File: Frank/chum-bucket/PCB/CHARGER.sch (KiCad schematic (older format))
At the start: 34 parts

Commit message: minor schematic update + inrush sim
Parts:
- added C? (x2): 0.1uF, symbol Device:C_Small
- added R? (x4): 0, symbol Device:R
- added U? (x2): INA196, Package_TO_SOT_SMD:SOT-23-5, symbol Amplifier_Current:INA196
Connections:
- net labels added: +3.3V, ANALOG_I_CHG, ANALOG_I_SYS, I_CHG_JMP_N, I_CHG_JMP_P, I_SYS_JMP_N, I_SYS_JMP_P
- wire segments 104 -> 124
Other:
- note added: "- Current amplifiers are 20V/V\n- Expected max output voltage is 2V (10A)\n- Protection and filtering on MCU page\n- Jumpers placed in case input impedance\n in case input impedance is too low \n and trips the charger"
- moved on the sheet: C?, D?, L?, Q?, R?, U?

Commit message: Weekends work. Final component selection then ready for review :)
huge oof
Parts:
- removed C?: 0.1uF, symbol Device:C_Small
- removed C?: 0.1u, symbol Device:C_Small
- removed D? (x2): BU, symbol Device:LED_Small
- removed Q?: Q_NMOS_DGS, symbol Device:Q_NMOS_DGS
- removed Q?: Q_PMOS_DGS, symbol Device:Q_PMOS_DGS
- removed R? (x2): 0, symbol Device:R
- removed R?: 1k, symbol Device:R_Small
- removed R?: 100k, symbol Device:R_Small
- removed U?: INA196, Package_TO_SOT_SMD:SOT-23-5, symbol Amplifier_Current:INA196
- added C? (x3): 100nF, symbol Device:C_Small
- added C?: 22nF, symbol Device:C_Small
- added C?: C, symbol Device:C_Small
- added D? (x2): GN, LED_SMD:LED_0603_1608Metric, symbol Device:LED_Small
- added F?: Fuse, symbol Device:Fuse
- added Q?: 2N7002K, Package_TO_SOT_SMD:SOT-23, symbol Transistor_FET:2N7002K
- added Q?: BSS84, Package_TO_SOT_SMD:SOT-23, symbol Transistor_FET:BSS84
- added R?: 330, symbol Device:R
- added R?: 100, symbol Device:R
- added R?: 4.7k, symbol Device:R_Small
- added R?: 1k, symbol Device:R_Small
- added R?: 10k, symbol Device:R_Small
- added R?: 430k, symbol Device:R
- added R?: 9.31k, symbol Device:R
- added R?: 5.1k, symbol Device:R
- added R?: 1k, symbol Device:R
- added R? (x2): 0, symbol Device:R_Small
- added TH?: NTC_TERM, Resistor_SMD:R_0603_1608Metric, symbol Device:Thermistor_NTC
- added U?: BTS6142DAUMA1, Package_TO_SOT_SMD:TO-252-4, symbol chum-bucket:BTS6142DAUMA1
- C?: value C_Small -> 1uF
- D?: value BU -> GN; footprint (none) -> LED_SMD:LED_0603_1608Metric; Digikey (none) -> 732-4971-2-ND
- R? (x2): value 100k -> 4.7k; Tolerance (none) -> 0.1%
- R?: value 32.4k -> 4.7k; Tolerance (none) -> 0.1%
- R?: value 100k -> ??; Tolerance (none) -> 0.1%
- R?: value 32.4k -> ??; Tolerance (none) -> 0.1%
- R?: value 32.4k -> 6.8k; Tolerance (none) -> 0.1%
- R?: value R -> 10m
- R? (x3): value 10k -> 1k
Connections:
- net labels added: +3V3, +BATT, AC_DRV, VREF, ~AC_DRV, ~BQ24617_BATT_DRV, ~CHG_LS_EN
- net labels removed: I_SYS_JMP_N, I_SYS_JMP_P
- wire segments 124 -> 164
- no-connect marks 0 -> 2
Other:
- note added: "- Current amplifier is 20V/V\n- Expected max output voltage is 2V (10A)\n- Protection and filtering on MCU page\n- Jumpers place in case BQ current sense input impedance is low"
- note added: "Final charge voltage set using this voltage divider\nV_bat = 2.1 * (1+R_top/R_bot)\nV_bat = 4.2*3 = 12.6\n12.6 * 2.1 - 1 = 5 = R_top/R_bot"
- note added: "Inverter glue logic for charger IC to supply load switch"
- note added: "Max IS current is 10mA under fault.\n330 ohm means max voltage of 3.1V"
- note added: "Option for thermistor. \nDNC for initial build\nVoltage div is dummy therm for testing"
- note added: "RIN_1 controls slew\nrate of the system bus"
- note added: "TTC pin sets time limit on charge\n0.01uF = 1 hour\n0.11uF = 10 hours\n5.6 min/nF\nCells should be 0.5C charge so we gucci w/ 2 hour"
- note removed: "- Current amplifiers are 20V/V\n- Expected max output voltage is 2V (10A)\n- Protection and filtering on MCU page\n- Jumpers placed in case input impedance\n in case input impedance is too low \n and trips the charger"
- note removed: "To do: Convert to load switch, use glue logic w/ stm"
- note removed: "To do: add load switch to turn pack onto system rail"
- moved on the sheet: C?, R?, U?

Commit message: batt-management sheet updates
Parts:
- added C? (x3): 10u, symbol Device:C_Small
- gave numbers to parts that had none: 1
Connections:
- wire segments 164 -> 173
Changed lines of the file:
@@
 SYS_PWR_OUT
 Wire Wire Line
-	4300 1100 6700 1100
+	4300 1100 5550 1100
 Wire Wire Line
 	4000 2050 4000 1100
@@
 ANALOG_I_SYS
 $Comp
-L Device:R R?
+L Device:R RIN_1
 U 1 1 5F19E549
 P 1600 6500
-F 0 "R?" H 1670 6546 50  0000 L CNN
+F 0 "RIN_1" H 1670 6546 50  0000 L CNN
 F 1 "100" H 1670 6455 50  0000 L CNN
 F 2 "" V 1530 6500 50  0001 C CNN
@@
 	-1   0    0    1
 $EndComp
+Wire Wire Line
+	6150 1450 6150 1400
+Wire Wire Line
+	5850 1450 5850 1400
+Wire Wire Line
+	5550 1450 5550 1400
+$Comp
+L power:GND #PWR?
+U 1 1 5F305781
+P 6150 1450
+AR Path="/5ECF1AA9/5F305781" Ref="#PWR?"  Part="1"
+AR Path="/5F305781" Ref="#PWR?"  Part="1"
+F 0 "#PWR?" H 6150 1200 50  0001 C CNN
+F 1 "GND" H 6155 1277 50  0000 C CNN
+F 2 "" H 6150 1450 50  0001 C CNN
+F 3 "" H 6150 1450 50  0001 C CNN
+	1    6150 1450
+	1    0    0    -1
+$EndComp
+$Comp
+L power:GND #PWR?
+U 1 1 5F305787
+P 5850 1450
+AR Path="/5ECF1AA9/5F305787" Ref="#PWR?"  Part="1"
+AR Path="/5F305787" Ref="#PWR?"  Part="1"
+F 0 "#PWR?" H 5850 1200 50  0001 C CNN
+F 1 "GND" H 5855 1277 50  0000 C CNN
+F 2 "" H 5850 1450 50  0001 C CNN
+F 3 "" H 5850 1450 50  0001 C CNN
+	1    5850 1450
+	1    0    0    -1
+$EndComp
+$Comp
+L power:GND #PWR?
+U 1 1 5F30578D
+P 5550 1450
+AR Path="/5ECF1AA9/5F30578D" Ref="#PWR?"  Part="1"
+AR Path="/5F30578D" Ref="#PWR?"  Part="1"
+F 0 "#PWR?" H 5550 1200 50  0001 C CNN
+F 1 "GND" H 5555 1277 50  0000 C CNN
+F 2 "" H 5550 1450 50  0001 C CNN
+F 3 "" H 5550 1450 50  0001 C CNN
+	1    5550 1450
+	1    0    0    -1
+$EndComp
+$Comp
+L Device:C_Small C?
+U 1 1 5F305793
+P 6150 1300
+AR Path="/5ECF1AA9/5F305793" Ref="C?"  Part="1"
+AR Path="/5F305793" Ref="C?"  Part="1"
+F 0 "C?" H 6058 1254 50  0000 R CNN
+F 1 "10u" H 6058 1345 50  0000 R CNN
+F 2 "" H 6150 1300 50  0001 C CNN
+F 3 "~" H 6150 1300 50  0001 C CNN
+	1    6150 1300
+	1    0    0    1
+$EndComp
+$Comp
+L Device:C_Small C?
+U 1 1 5F305799
+P 5850 1300
+AR Path="/5ECF1AA9/5F305799" Ref="C?"  Part="1"
+AR Path="/5F305799" Ref="C?"  Part="1"
+F 0 "C?" H 5758 1254 50  0000 R CNN
+F 1 "10u" H 5758 1345 50  0000 R CNN
+F 2 "" H 5850 1300 50  0001 C CNN
+F 3 "~" H 5850 1300 50  0001 C CNN
+	1    5850 1300
+	1    0    0    1
+$EndComp
+$Comp
+L Device:C_Small C?
+U 1 1 5F30579F
+P 5550 1300
+AR Path="/5ECF1AA9/5F30579F" Ref="C?"  Part="1"
+AR Path="/5F30579F" Ref="C?"  Part="1"
+F 0 "C?" H 5458 1254 50  0000 R CNN
+F 1 "10u" H 5458 1345 50  0000 R CNN
+F 2 "" H 5550 1300 50  0001 C CNN
+F 3 "~" H 5550 1300 50  0001 C CNN
+	1    5550 1300
+	1    0    0    1
+$EndComp
+Wire Wire Line
+	5550 1200 5550 1100
+Connection ~ 5550 1100
+Wire Wire Line
+	5550 1100 5850 1100
+Wire Wire Line
+	5850 1200 5850 1100
+Connection ~ 5850 1100
+Wire Wire Line
+	5850 1100 6150 1100
+Wire Wire Line
+	6150 1200 6150 1100
+Connection ~ 6150 1100
+Wire Wire Line
+	6150 1100 6700 1100
 $EndSCHEMATC

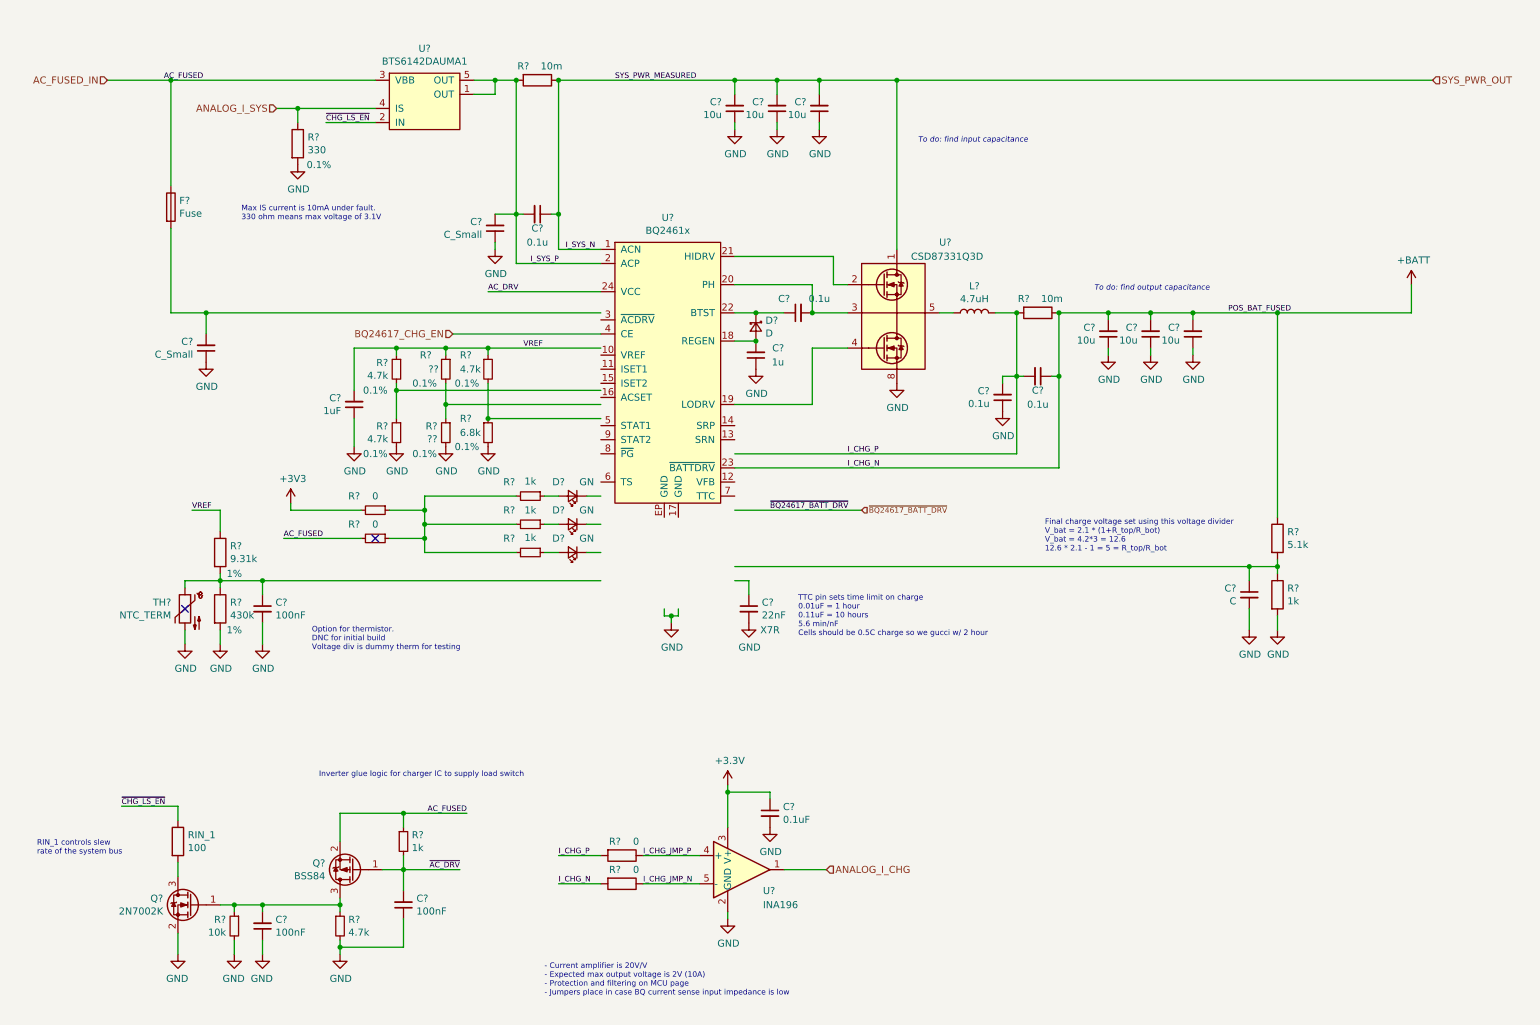
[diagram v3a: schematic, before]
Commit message: Minor schematic organization changes
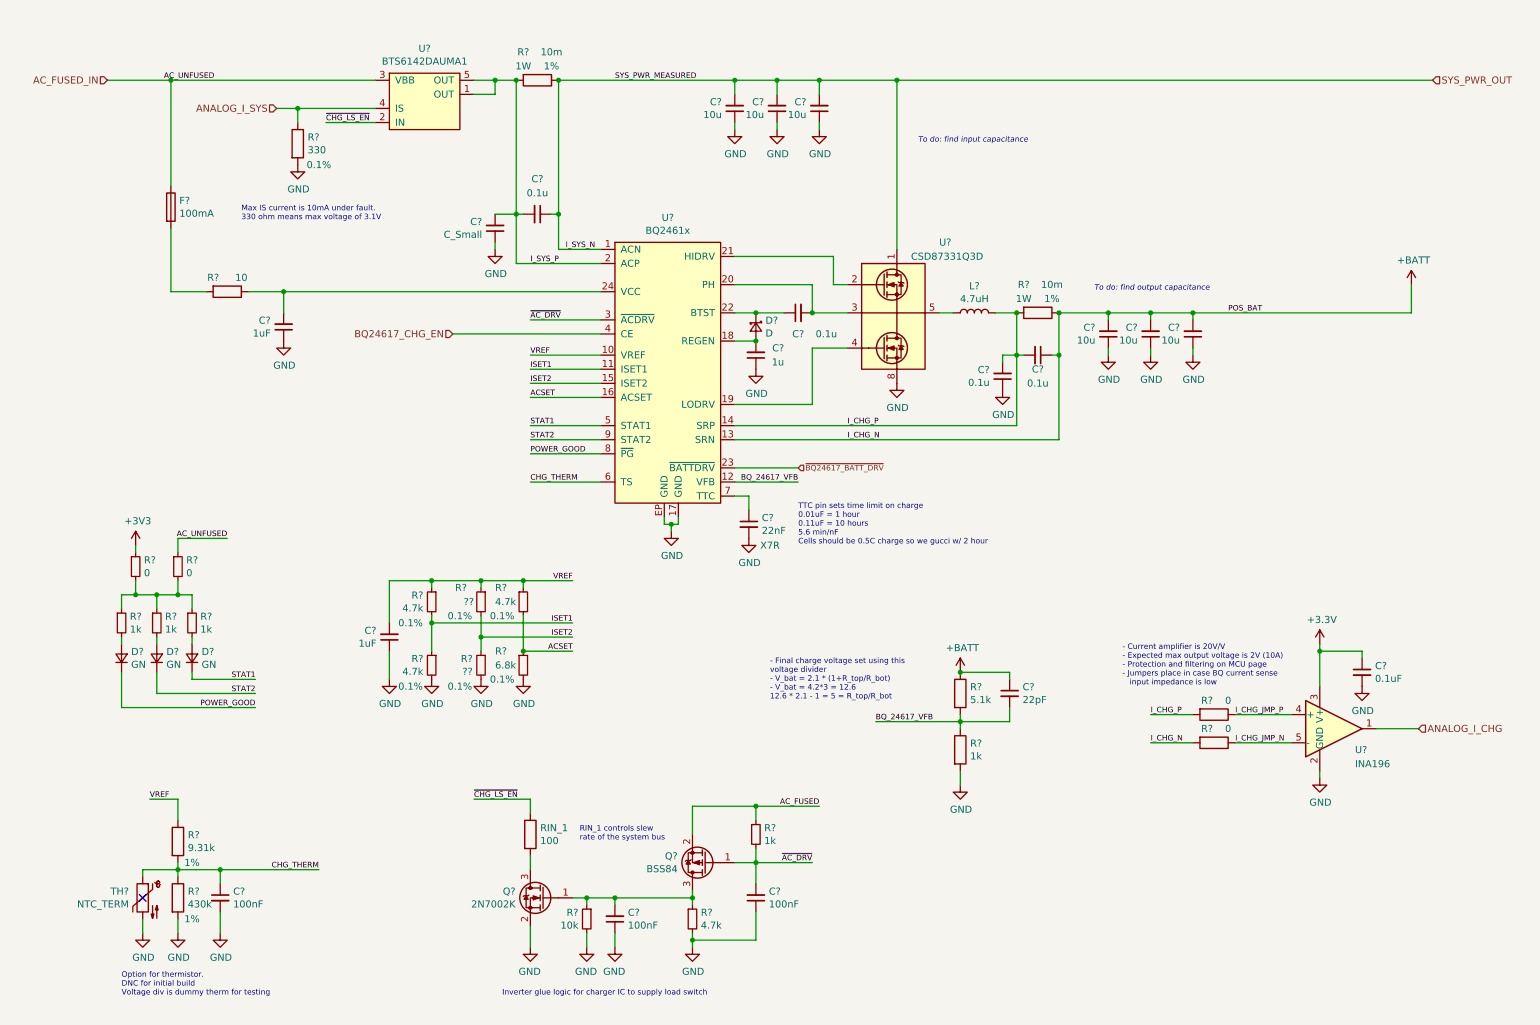
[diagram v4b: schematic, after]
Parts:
- removed D? (x3): GN, LED_SMD:LED_0603_1608Metric, symbol Device:LED_Small
- removed R? (x2): 0, symbol Device:R_Small
- removed R?: 10m, symbol Device:R
- removed R? (x3): 1k, symbol Device:R_Small
- added D? (x3): GN, symbol Device:D_Small
- added R? (x2): 0, symbol Device:R_Small
- added R? (x3): 1k, symbol Device:R_Small
- added R?: 10, symbol Device:R
- added R?: 10m, Resistor_SMD:R_2512_6332Metric_Pad1.52x3.35mm_HandSolder, symbol Device:R
- C?: value C -> 22pF
- C?: value C_Small -> 1uF
- F?: value Fuse -> 100mA
- R?: footprint (none) -> Resistor_SMD:R_2512_6332Metric_Pad1.52x3.35mm_HandSolder; Digikey (none) -> YAG2167TR-ND; Power (none) -> 1W; Tolerancw (none) -> 1%
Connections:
- net labels added: ACSET, AC_UNFUSED, BQ_24617_VFB, CHG_THERM, ISET1, ISET2, POS_BAT, POWER_GOOD, STAT1, STAT2
- net labels removed: AC_DRV, POS_BAT_FUSED
- wire segments 173 -> 185
- no-connect marks 2 -> 1
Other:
- note added: "- Current amplifier is 20V/V\n- Expected max output voltage is 2V (10A)\n- Protection and filtering on MCU page\n- Jumpers place in case BQ current sense \n input impedance is low"
- note added: "- Final charge voltage set using this \nvoltage divider\n- V_bat = 2.1 * (1+R_top/R_bot)\n- V_bat = 4.2*3 = 12.6\n12.6 * 2.1 - 1 = 5 = R_top/R_bot"
- note removed: "- Current amplifier is 20V/V\n- Expected max output voltage is 2V (10A)\n- Protection and filtering on MCU page\n- Jumpers place in case BQ current sense input impedance is low"
- note removed: "Final charge voltage set using this voltage divider\nV_bat = 2.1 * (1+R_top/R_bot)\nV_bat = 4.2*3 = 12.6\n12.6 * 2.1 - 1 = 5 = R_top/R_bot"
- moved on the sheet: C?, Q?, R?, RIN_1, TH?, U?

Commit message: for review at 2pm
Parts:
- removed C? (x6): 10u, symbol Device:C_Small
- removed R?: 10m, Resistor_SMD:R_2512_6332Metric_Pad1.52x3.35mm_HandSolder, symbol Device:R
- added C? (x9): 4.7uF, Capacitor_SMD:C_1210_3225Metric, symbol Device:C_Small
- added R?: 10m, Resistor_SMD:R_1206_3216Metric, symbol Device:R
- C?: value 1u -> 1uF; Voltage (none) -> 6V
- R?: footprint Resistor_SMD:R_2512_6332Metric_Pad1.52x3.35mm_HandSolder -> Resistor_SMD:R_1206_3216Metric; Digikey YAG2167TR-ND -> CRF1206-FZ-R010ELFTR-ND
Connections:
- net +BATT: now also C?.2, C?.2, C?.2, R?.1
- net GND: now also C?.1, C?.1, C?.1, C?.1, C?.1, C?.1, C?.1, C?.1, C?.1
- net I_CHG_P: now also R?.2
- net SYS_PWR_OUT: now also C?.2, C?.2, C?.2, C?.2, C?.2, C?.2
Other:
- note removed: "To do: find input capacitance"
- note removed: "To do: find output capacitance"

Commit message: more work
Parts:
- removed C? (x9): 4.7uF, Capacitor_SMD:C_1210_3225Metric, symbol Device:C_Small
- removed C?: 0.1uF, symbol Device:C_Small
- removed C? (x2): 100nF, symbol Device:C_Small
- removed C?: 1uF, symbol Device:C_Small
- removed C? (x2): 0.1u, symbol Device:C_Small
- removed D? (x2): GN, symbol Device:D_Small
- removed R?: 0, symbol Device:R_Small
- removed R? (x3): 1k, symbol Device:R_Small
- removed R?: 10k, symbol Device:R_Small
- removed R?: ??, symbol Device:R_Small
- removed R?: 4.7k, symbol Device:R_Small
- added C101: 1uF, Capacitor_SMD:C_0805_2012Metric, symbol Device:C_Small
- added C106, C110, C112, C116, C117: 10uF, Capacitor_SMD:C_2220_5650Metric, symbol Device:C
- added C108, C113, C114: 0.1uF, Capacitor_SMD:C_0603_1608Metric, symbol Device:C_Small
- added C115: 0.1u, Capacitor_SMD:C_0603_1608Metric, symbol Device:C_Small
- added C118: 10nF, Capacitor_SMD:C_0603_1608Metric, symbol Device:C_Small
- added D102, D103: GN, LED_SMD:LED_0603_1608Metric, symbol Device:D_Small
- added R105, R108: 10k, Resistor_SMD:R_0603_1608Metric, symbol Device:R_Small
- added R113, R115, R123, R125: 1k, Resistor_SMD:R_0603_1608Metric, symbol Device:R_Small
- added R114: 0, Resistor_SMD:R_0603_1608Metric, symbol Device:R_Small
- added R121: 100, Resistor_SMD:R_0603_1608Metric, symbol Device:R
- C102: renamed from C?; footprint (none) -> Capacitor_SMD:C_0603_1608Metric; Digikey (none) -> 399-7874-2-ND; Voltage (none) -> 25V
- C103: renamed from C?; footprint (none) -> Capacitor_SMD:C_0805_2012Metric; Voltage (none) -> 25V
- C104: renamed from C?; value C_Small -> 0.1uF; footprint (none) -> Capacitor_SMD:C_0603_1608Metric; Digikey (none) -> 399-7845-2-ND
- C105: renamed from C?; footprint (none) -> Capacitor_SMD:C_0603_1608Metric; Digikey (none) -> 399-7845-2-ND
- C107: renamed from C?; footprint (none) -> Capacitor_SMD:C_0805_2012Metric; Digikey (none) -> 490-1644-2-ND; Tolerance X7R -> C0G
- C109: renamed from C?; footprint (none) -> Capacitor_SMD:C_0805_2012Metric
- C111: renamed from C?; footprint (none) -> Capacitor_SMD:C_0603_1608Metric; Digikey (none) -> 399-7845-2-ND; Voltage (none) -> 25V
- C119: renamed from C?; value 100nF -> 10nF; footprint (none) -> Capacitor_SMD:C_0603_1608Metric; Digikey (none) -> 399-7842-2-ND; Voltage (none) -> 25V
- D101: renamed from D?; footprint (none) -> LED_SMD:LED_0603_1608Metric; Digikey (none) -> 160-1446-2-ND
- D104: renamed from D?; value D -> BAT54T1G; footprint (none) -> Diode_SMD:D_SOD-123F; Digikey (none) -> BAT54T1GOSTR-ND
- F101: renamed from F?; footprint (none) -> Fuse:Fuse_0603_1608Metric; Digikey (none) -> 478-6872-2-ND
- R101: renamed from R?; value 4.7k -> 10k; footprint (none) -> Resistor_SMD:R_0603_1608Metric
- R102: renamed from R?; value 4.7k -> 3.3k
- R103: renamed from R?; value 5.1k -> 499k; footprint (none) -> Resistor_SMD:R_0603_1608Metric; Tolerance (none) -> 0.1%
- R104: renamed from R?; value 1k -> 100k; footprint (none) -> Resistor_SMD:R_0603_1608Metric; Tolerance (none) -> 0.1%
- R106: renamed from R?; value ?? -> 330
- R107: renamed from R?; footprint (none) -> Resistor_SMD:R_0603_1608Metric; Digikey (none) -> 541-10UATR-ND; Power (none) -> 0.1W
- R109: renamed from R?; value 6.8k -> 15k
- R110: renamed from R?; footprint (none) -> Resistor_SMD:R_0603_1608Metric; Digikey (none) -> P19915TR-ND; Power (none) -> 0.1W
- R111, R112, R117, R118, R119, R120: renamed from R?; footprint (none) -> Resistor_SMD:R_0603_1608Metric
- R124: renamed from R?; footprint (none) -> Resistor_SMD:R_0603_1608Metric; Digikey (none) -> RHM4.7DTR-ND
- RIN_1: footprint (none) -> Resistor_SMD:R_0603_1608Metric; Digikey (none) -> 311-100HRTR-ND; Percentage 0.1% -> 1%
- gave numbers to parts that had none: 10
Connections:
- net +3V3: now also C108.2
- net +BATT: now also C115.1, C116.1, C117.1
- net ACSET: now also R108.2
- net AC_FUSED: now also R125.1
- net AC_FUSED_IN: now also R114.1
- net CHG_THERM: now also C113.2, R121.2; no longer R119.2, R120.1, TH101.1
- net GND: now also C101.1, C106.2, C108.1, C110.2, C112.2, C113.1, C114.1, C116.2, C117.2, C118.1, R123.2
- net ISET2: now also R105.2
- net I_CHG_P: now also C114.2, C115.2
- net STAT1: now also D103.1 (K)
- net STAT2: now also D102.1 (K)
- net SYS_PWR_OUT: now also C106.1, C110.1, C112.1
- net VREF: now also C101.2, R105.1, R108.1
- net ~AC_DRV: now also R125.2
- net at Q101.1 (G), Q102.3 (D), R124.1: now also C118.2, R123.1
- net at R111.1, R112.2: now also R113.1, R114.2, R115.1
- new net: D102.2 (A), R113.2
- new net: D103.2 (A), R115.2
- new net: R119.2, R120.1, R121.1, TH101.1
- no-connect marks 1 -> 2
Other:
- note added: "- Current amplifier is 20V/V\n- Expected max output voltage is 2V (10A)\n- Protection and filtering on MCU page\n- Jumpers place in case BQ current sense \n input impedance is low\n- Bandwidth of 500kHz so may alias waveform"
- note added: "- ISET1 sets max current during charge (0.5C*8A = 4A)\n- ISET2 sets precharge AND termination charge current (100mA)\n- ACSET sets the max AC adapter current (10A)"
- note added: "- VREF = 3.3V\n- V_ISET1 = I_CHG * 20 * RSR = 0.8V\n- V_ISET2 = I_TERM * 100 * RSR = 0.1V\n- V_ACSET = I_AC * 20 * R_AC = 2V"
- note added: "<----- Load Switch | Charger IC ----->"
- note added: "Option for thermistor. \nDNC for initial build\nJust pop. voltage div. as dummy therm. \nFilter 3db freq: 16kHz"
- note added: "Option to choose LED power. \nUse 10kOhm for AC_Adapter"
- note added: "VCC max current is 25mA\nI^R = .025*.025*10 < 0.1W"
- note removed: "- Current amplifier is 20V/V\n- Expected max output voltage is 2V (10A)\n- Protection and filtering on MCU page\n- Jumpers place in case BQ current sense \n input impedance is low"
- note removed: "Option for thermistor. \nDNC for initial build\nVoltage div is dummy therm for testing"
- moved on the sheet: C102, C119, D101, Q101, Q102, R101, R102, R103, R104, R106, R109, R111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

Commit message: changes
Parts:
- added TP? (x2): VFB, TestPoint:TestPoint_Pad_D1.0mm, symbol Connector:TestPoint
- added TP?: SW_NODE, TestPoint:TestPoint_Pad_D1.0mm, symbol Connector:TestPoint
- U103: value CSD87331Q3D -> CSD87331
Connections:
- net BQ_24617_VFB: now also TP?.1
- net CHG_THERM: now also TP?.1
- net at L101.1, U103.5 (VSW): now also TP?.1
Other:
- moved on the sheet: C101, C112, D101, D102, D103, R101, R102, R105, R106, R108, R109, R111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
